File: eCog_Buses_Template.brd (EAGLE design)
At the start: 45.5 x 27.9 mm, 1 part

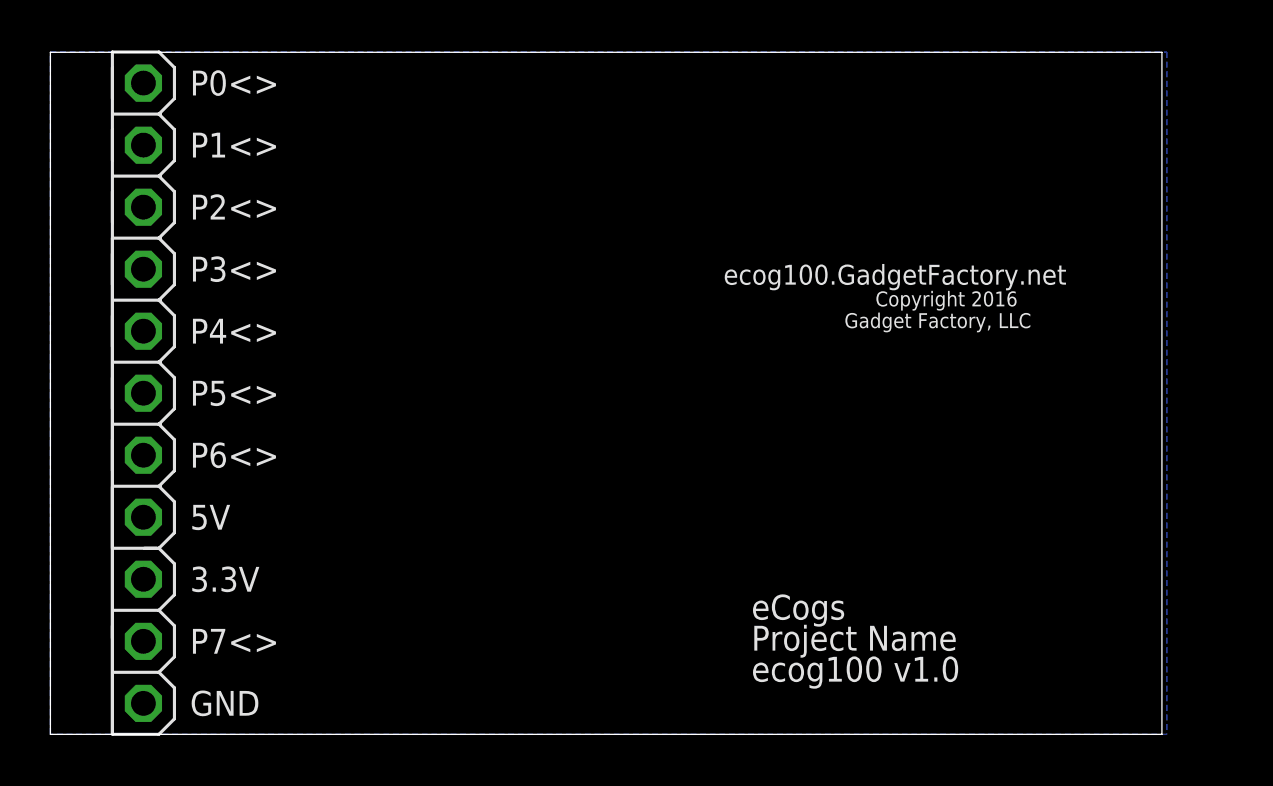
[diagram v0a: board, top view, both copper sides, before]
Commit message: Update library and templates for surface mount pin headers.
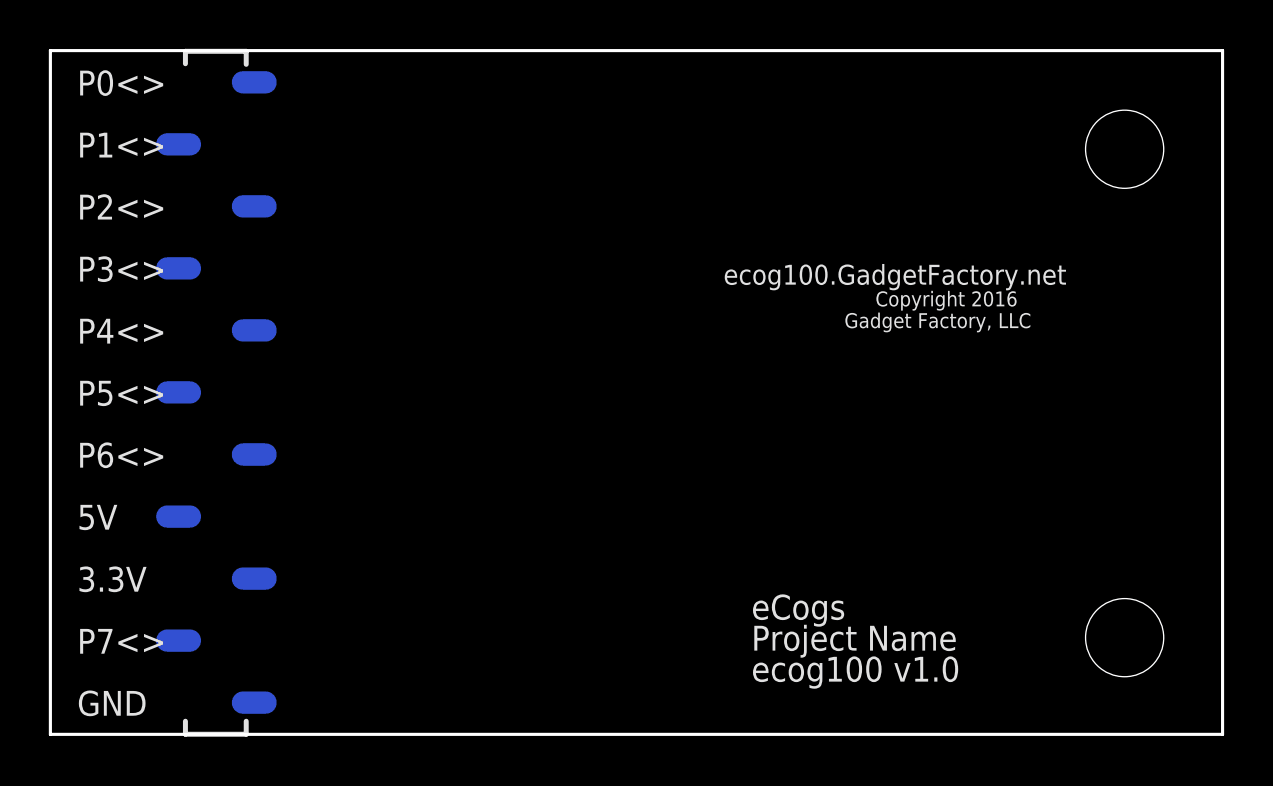
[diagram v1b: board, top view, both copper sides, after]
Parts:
- ECOG: value ECOG_BUSES_ROW -> ECOG_BUSES_ROWECOG_BUSES_SMD; device eCogs:ECOG_BUSES_ROW -> eCogs:ECOG_BUSES_SMD
- moved ECOG 28.1 mm to (0.00, 0.00), turned to 0 degrees
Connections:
- net GND: now also ECOG.P$11; no longer ECOG.GND@2
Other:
- board size 45.5 x 27.9 mm -> 48 x 28 mm

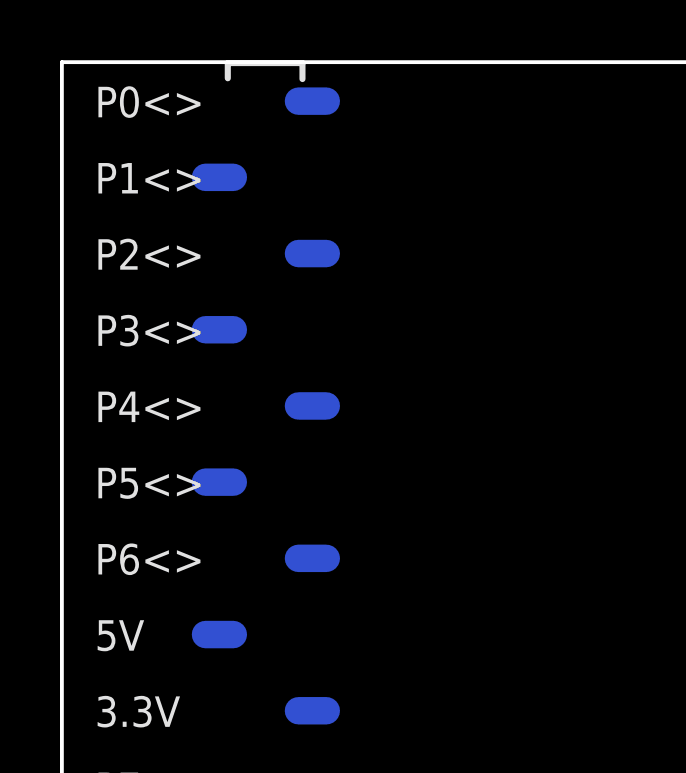
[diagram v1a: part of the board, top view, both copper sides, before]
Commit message: Update pin names for the buses
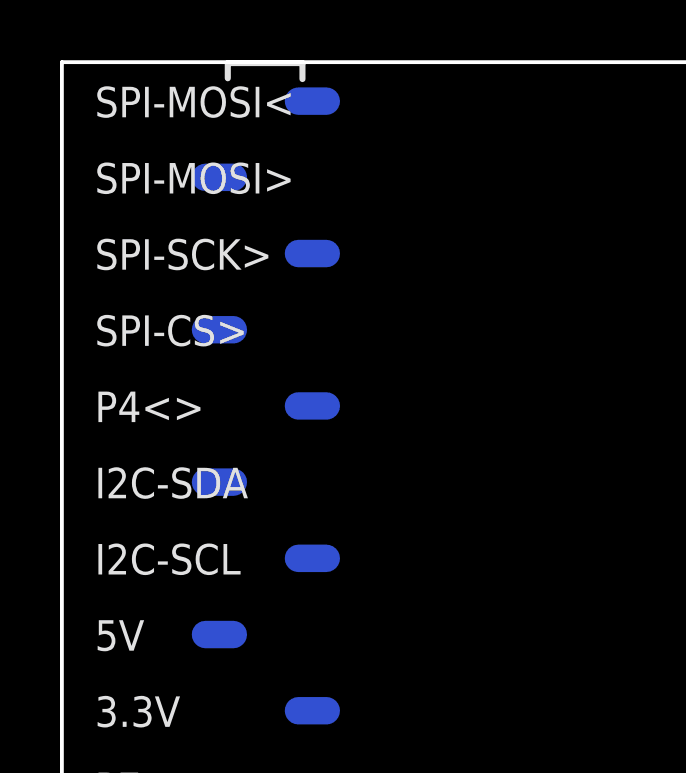
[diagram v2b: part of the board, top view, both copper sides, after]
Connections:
- net GND: now also ECOG.GND; no longer ECOG.P$11
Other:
- board text added: "I2C-SCL"
- board text added: "I2C-SDA"
- board text added: "SPI-CS>"
- board text added: "SPI-MOSI<"
- board text added: "SPI-MOSI>"
- board text added: "SPI-SCK>"
- board text removed: "P0<>"
- board text removed: "P1<>"
- board text removed: "P2<>"
- board text removed: "P3<>"
- board text removed: "P5<>"
- board text removed: "P6<>"
